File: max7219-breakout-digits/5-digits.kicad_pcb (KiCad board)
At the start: 2 copper layers, 60 x 12 mm, 6 parts, among them J1 Conn_02x08_Odd_Even, U1 7Segment 3 digit CC_STH, U2 HDSM-443B_CC_2Digit_7Segment_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

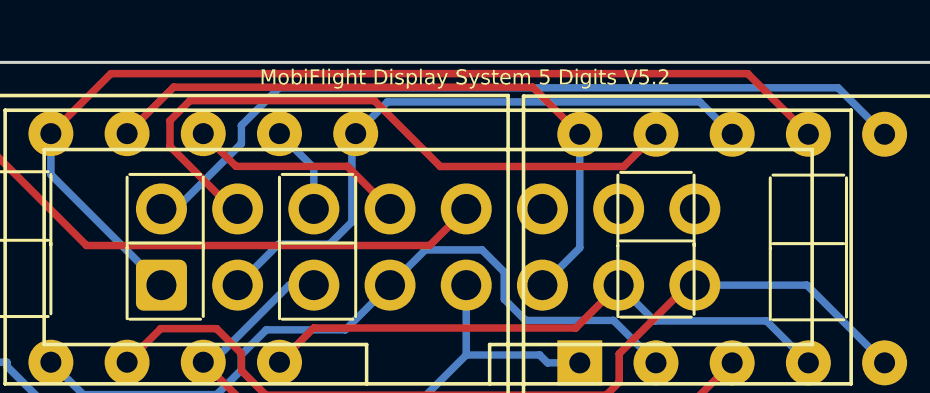
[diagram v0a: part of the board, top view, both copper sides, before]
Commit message: MF Logo on correct positions, wrong link deleted
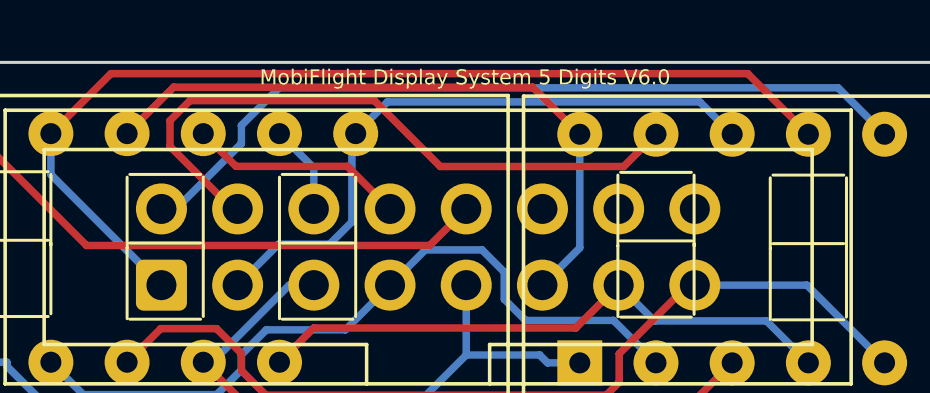
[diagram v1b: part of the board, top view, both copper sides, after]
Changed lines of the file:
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@@
 	(title_block
 		(title "7 Segment Display Module, 5 digits")
-		(date "2025-11")
-		(rev "V5.2")
+		(date "2025-12")
+		(rev "V6.0")
 		(company "MobiFlight")
 	)

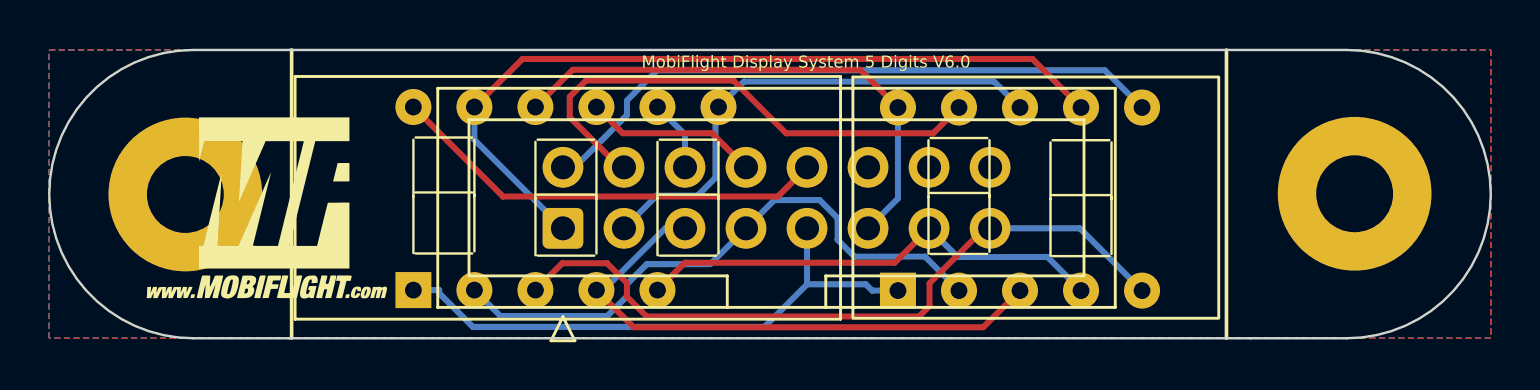
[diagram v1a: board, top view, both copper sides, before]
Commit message: fixed IDC connector on wrong side for 3 and 5 digit
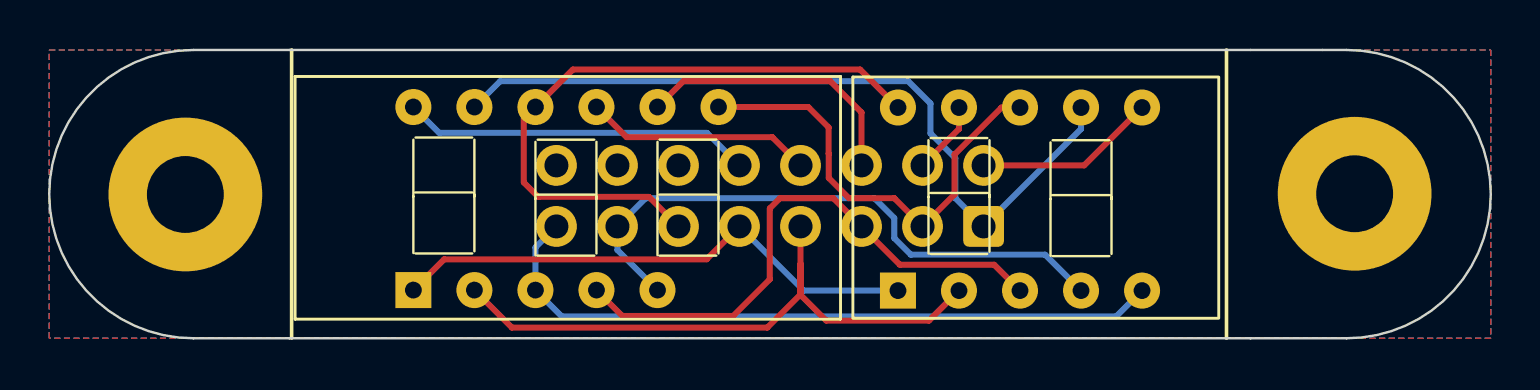
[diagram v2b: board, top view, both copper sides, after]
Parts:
- G2, J1: moved to B.Cu
- moved G2 41.0 mm to (116.1, 69.0), turned to 180 degrees
- moved J1 17.5 mm to (105.0, 68.4)
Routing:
- net /DIG0: track 26.8 -> 7.59 mm
- net /DIG1: track 21.8 -> 3.04 mm
- net /DIG2: track 2.98 -> 11.7 mm
- net /G: track 19.8 -> 25.2 mm
- net /F: track 21.9 -> 26.9 mm
- net /DIG4: track 18.4 -> 14.6 mm
- net /B: track 21.1 -> 18.9 mm
- net /DIG3: track 7.26 -> 9.50 mm
- net /E: track 24.1 -> 22.4 mm
- net /D: track 25.0 -> 26.5 mm
- net /A: track 33.5 -> 32.5 mm
- net /DP: track 30.1 -> 29.2 mm

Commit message: slight movement of mounting holes to get full millimeters
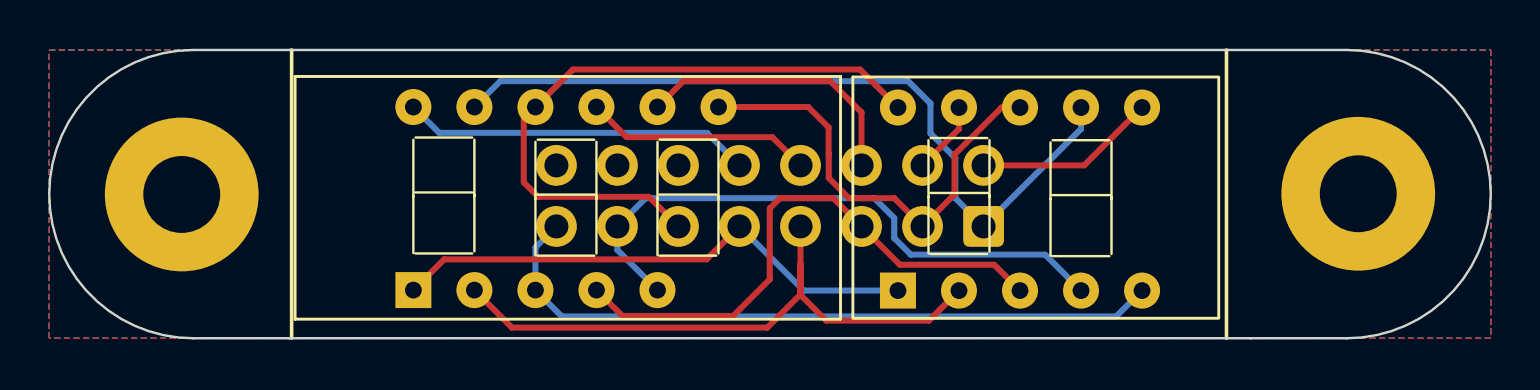
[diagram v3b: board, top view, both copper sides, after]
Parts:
- moved H2 0.15 mm to (120.6, 67.0)
- moved H1 0.15 mm to (71.6, 67.0)
- moved G2 0.14 mm to (116.0, 69.0)
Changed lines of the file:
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@@
 	(footprint "MountingHole:MountingHole_3.2mm_M3_Pad"
 		(layer "F.Cu")
-		(at 120.4434 67.0104)
+		(at 120.5934 67.0104)
 		(descr "Mounting Hole 3.2mm, M3, generated by kicad-footprint-generator mountinghole.py")
 		(tags "mountinghole M3")
@@
 	(footprint "MountingHole:MountingHole_3.2mm_M3_Pad"
 		(layer "F.Cu")
-		(at 71.7734 67.0404)
+		(at 71.6234 67.0404)
 		(descr "Mounting Hole 3.2mm, M3, generated by kicad-footprint-generator mountinghole.py")
 		(tags "mountinghole M3")
@@
 	(footprint "MobiFlight:MobiFlight-Logo-Small"
 		(layer "B.Cu")
-		(at 116.14 68.97 180)
+		(at 115.999422 68.962353 180)
 		(property "Reference" "G2"
 			(at 0 0 0)
@@
 	)
 	(group ""
-		(members "7358d4fd-9024-47a7-9c53-15a8ffe03d2a" "d40def2e-617a-4ba2-a011-fcf9c19e2675")
-	)
-	(group ""
